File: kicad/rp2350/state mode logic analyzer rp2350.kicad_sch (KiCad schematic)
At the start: 152 parts, among them J1 USB0, J2 5V USB0, J3 Probe_Hi, J4 Probe Power, J5 Probe_Lo, J6 Probe Power, J7 SWD0, SW1 Reset 0, SW2 Boot 0, U1 NCP1117-ADJ_SOT223, U12 SN74LVC8T245, U13 SN74LVC2T45DCUR, U2 RP2350_80QFN, U3 AD5241BRZ1M, U4 SN74LVC8T245, U5 SN74LVC8T245, U6 SN74LVC8T245, U7 IS25LP128F-JBLE, U9 MCP1826S, Y1 ECS-120-18-33-JEM-TR

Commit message: replaced discrete rp2350 with stampxl (schematic only)
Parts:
- removed C1, C2: 27p, Capacitor_SMD:C_0603_1608Metric, symbol Device:C
- removed C13, C15, C16, C17, C18, C25, C26, C27, C28, C29, C30: 100n, Capacitor_SMD:C_0402_1005Metric, symbol Device:C
- removed C14, C34: 4.7u, Capacitor_SMD:C_0402_1005Metric, symbol Device:C
- removed C31: 1u, Capacitor_SMD:C_0603_1608Metric_Pad1.08x0.95mm_HandSolder, symbol Device:C_Small
- removed C32, C33: 4.7u, RP2350_80QFN_minimal:C_0402_1005Metric_small_pads, symbol Device:C
- removed C5: 10u, Capacitor_SMD:C_0805_2012Metric, symbol My Library:C_0805
- removed C6: 1u, Capacitor_SMD:C_0805_2012Metric, symbol My Library:C_0805
- removed D3: 1v1, LED_SMD:LED_1206_3216Metric_Pad1.42x1.75mm_HandSolder, symbol Device:LED_Small_Filled
- removed D7: BZA856AVL, Package_TO_SOT_SMD:SOT-353_SC-70-5, symbol Power_Protection:SP0504BAJT
- removed J1: USB0, Connector_USB:USB_C_Receptacle_GCT_USB4105-xx-A_16P_TopMnt_Horizontal, symbol Connector:USB_C_Receptacle_USB2.0_16P
- removed L1: 3.3u, RP2350_80QFN_minimal:L_pol_2016, symbol Device:L
- removed R10: 1k, Resistor_SMD:R_0603_1608Metric_Pad0.98x0.95mm_HandSolder, symbol Device:R_Small
- removed R12: 0, Resistor_SMD:R_0603_1608Metric_Pad0.98x0.95mm_HandSolder, symbol Device:R
- removed R16, R17: 27, Resistor_SMD:R_0603_1608Metric_Pad0.98x0.95mm_HandSolder, symbol Device:R_Small
- removed R23, R24: 5k1, Resistor_SMD:R_0603_1608Metric_Pad0.98x0.95mm_HandSolder, symbol Device:R_Small
- removed R44: 33, Resistor_SMD:R_0402_1005Metric, symbol Device:R
- removed TP15: TestPoint_Harwin, My Libraries:Harwin-S1751-46-Test-Point, symbol My Library:TestPoint_Harwin
- removed U2: RP2350_80QFN, RP2350_80QFN_minimal:RP2350-QFN-80-1EP_10x10_P0.4mm_EP3.4x3.4mm_ThermalVias, symbol MCU_RaspberryPi_RP2350:RP2350_80QFN
- removed U7: IS25LP128F-JBLE, Package_SO:SOIC-8_5.23x5.23mm_P1.27mm, symbol Memory_Flash:W25Q128JVS
- removed U9: MCP1826S, Package_TO_SOT_SMD:SOT-223, symbol Regulator_Linear:MCP1826S
- removed Y1: ECS-120-18-33-JEM-TR, Crystal:Crystal_SMD_3225-4Pin_3.2x2.5mm, symbol Device:Crystal_GND24
- added D6: BZA856AVL, Package_TO_SOT_SMD:SOT-353_SC-70-5, symbol Power_Protection:SP0504BAJT
- added J1: USB0, Connector_USB:USB_C_Receptacle_GCT_USB4105-xx-A_16P_TopMnt_Horizontal, symbol Connector:USB_C_Receptacle_USB2.0
- added J8: FTDI Header, Connector_PinSocket_2.54mm:PinSocket_1x06_P2.54mm_Vertical, symbol Connector_Generic:Conn_01x06
- added R3, R4: 5k1, Resistor_SMD:R_0603_1608Metric_Pad0.98x0.95mm_HandSolder, symbol Device:R_Small
- added R9: 27, Resistor_SMD:R_0603_1608Metric_Pad0.98x0.95mm_HandSolder, symbol Device:R_Small
- added U2: RP2350_Stamp_XL, RP2xxx_Stamp:RP2xxx_Stamp_XL_THT, symbol RP2xxx_Stamp:RP2350_Stamp_XL
- J7: STANDARD Manufacturer Recommendation -> 01R3466
- R7: value 4k7 -> 1k
- R8: value 4k7 -> 27
- SW1: value Reset 0 -> Reset
- SW2: value Boot 0 -> Boot
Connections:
- net +3V3: now also U2.34 (3.3V); no longer R8.1
- net +5V: now also J8.3 (Pin_3), U2.33 (5V)
- net DN: now also R8.1, U2.35 (USB_D-)
- net DP: now also R9.1, U2.36 (USB_D+)
- net GND: now also D6.2 (A), J1.A1 (GND), J1.A12 (GND), J1.B1 (GND), J1.B12 (GND), J1.S1 (SHIELD), J8.1 (Pin_1), R3.2, R4.2, U2.31 (GND)
- net SWCLK: now also U2.38 (SWCLK)
- net SWD: now also U2.37 (SWDIO)
- net USB_DN: now also R8.2, D6.5 (K), J1.A7 (D-), J1.B7 (D-)
- net USB_DP: now also D6.4 (K), J1.A6 (D+), J1.B6 (D+), R9.2
- net VBUS: now also D6.3 (K), J1.A4 (VBUS), J1.A9 (VBUS), J1.B4 (VBUS), J1.B9 (VBUS)
- net at SW2.1: now also R7.2
- net +1V1: no longer names the net of R7.1
- net +1V1: now also U2.40 (BOOTSEL)
- net Run renamed Reset
- net Reset: now also U2.39 (~{RESET}); no longer R8.2
- new net: J1.B5 (CC2), R4.1
- new net: J1.A5 (CC1), R3.1
- new net UART_RX: J8.4 (Pin_4), U2.2 (GPIO1)
- new net UART_TX: J8.5 (Pin_5), U2.1 (GPIO0)
- no-connect marks 3 -> 8
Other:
- note removed: "Added hidden Pin 4 to MCP1826S Symbol"
- note removed: "MCU (RP2354b)"
- note removed: "Power"
- note removed: "TODO: Add PSRAM"
- moved on the sheet: D4, D5, D8, R1, R2, R41, R42, R43, TP21, TP22

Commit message: remove complicated Vccb supply circuit
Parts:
- added C1, C2: 10u, symbol Device:C_Small
- added C5: 1u, symbol Device:C_Small
- added C6: 1u, Capacitor_SMD:C_0603_1608Metric_Pad1.08x0.95mm_HandSolder, symbol Device:C_Small
- added J9: Vth_select, symbol Connector_Generic:Conn_01x03
- added R10: 3k3, symbol Device:R_Small
- added R11: 1k, symbol Device:R_Small
- added TP1, TP2, TP3, TP4, TP5, TP6: TestPoint_Harwin, My Libraries:Harwin-S1751-46-Test-Point, symbol My Library:TestPoint_Harwin
- D8: value 2040_L0 -> 2350_LED
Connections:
- net SCL is gone; now on net I2C1_SCL: R42.2, TP22.1
- net SDA is gone; now on net I2C1_SDA: R41.2, TP21.1
- net +3V3: now also U3.4 (VDD), U3.5 (~{SHDN}), C6.1, TP3.1; no longer U12.23 (V_{CCB}), U12.24 (V_{CCB}), U13.8 (VCCB), U4.23 (V_{CCB}), U4.24 (V_{CCB}), U5.23 (V_{CCB}), U5.24 (V_{CCB}), U6.23 (V_{CCB}), U6.24 (V_{CCB})
- net +5V: now also U1.3 (VI), C1.1, J9.3 (Pin_3)
- net BUF00: now also U2.46 (GPIO35)
- net BUF01: now also U2.45 (GPIO34)
- net BUF02: now also U2.44 (GPIO33)
- net BUF03: now also U2.43 (GPIO32)
- net BUF04: now also U2.42 (GPIO31)
- net BUF05: now also U2.41 (GPIO30)
- net BUF06: now also U2.30 (GPIO29)
- net BUF07: now also U2.29 (GPIO28)
- net BUF08: now also U2.28 (GPIO27)
- net BUF09: now also U2.27 (GPIO26)
- net BUF10: now also U2.26 (GPIO25)
- net BUF11: now also U2.25 (GPIO24)
- net BUF12: now also U2.24 (GPIO23)
- net BUF13: now also U2.23 (GPIO22)
- net BUF14: now also U2.22 (GPIO21)
- net BUF15: now also U2.21 (GPIO20)
- net BUF16: now also U2.18 (GPIO17)
- net BUF17: now also U2.17 (GPIO16)
- net BUF18: now also U2.16 (GPIO15)
- net BUF19: now also U2.15 (GPIO14)
- net BUF20: now also U2.14 (GPIO13)
- net BUF21: now also U2.13 (GPIO12)
- net BUF22: now also U2.12 (GPIO11)
- net BUF23: now also U2.11 (GPIO10)
- net BUF24: now also U2.10 (GPIO9)
- net BUF25: now also U2.9 (GPIO8)
- net BUF26: now also U2.8 (GPIO7)
- net BUF27: now also U2.7 (GPIO6)
- net BUF28: now also U2.6 (GPIO5)
- net BUF29: now also U2.5 (GPIO4)
- net BUF30: now also U2.4 (GPIO3)
- net BUF31: now also U2.3 (GPIO2)
- net CLK: now also U2.2 (GPIO1), U2.20 (GPIO19)
- net GND: now also U3.10 (GND), U3.11 (VSS), U3.3 (B), U3.8 (AD0), U3.9 (AD1), C1.2, C2.2, C5.2, C6.2, R11.2
- net QUAL: now also U2.1 (GPIO0), U2.19 (GPIO18)
- net UART_RX: now also U2.56 (GPIO45); no longer U2.2 (GPIO1)
- net UART_TX: now also U2.55 (GPIO44); no longer U2.1 (GPIO0)
- net at U3.1 (A): now also TP5.1
- net at U3.12 (O2): now also TP2.1
- net at U3.14 (O1): now also TP1.1
- net at U3.2 (W): now also U1.1 (ADJ), C5.1, R10.2, TP4.1
- net I2C1_SCL: now reaches U3.6 (SCL)
- net I2C1_SCL: now also U2.58 (GPIO47)
- net I2C1_SDA: now reaches U3.7 (SDA)
- net I2C1_SDA: now also U2.57 (GPIO46)
- net Vvar: now reaches U1.2 (VO)
- net Vvar: now also C2.1, J9.1 (Pin_1), R10.1, R11.1, TP6.1
- net 2350_LED: now reaches R43.1
- net 2350_LED: now also U2.53 (GPIO42)
- net Armed: now reaches U2.51 (GPIO40)
- net Armed: now also R1.1
- net Triggered: now reaches U2.52 (GPIO41)
- net Triggered: now also R2.1
- new net Vccb: J9.2 (Pin_2), U12.23 (V_{CCB}), U12.24 (V_{CCB}), U13.8 (VCCB), U4.23 (V_{CCB}), U4.24 (V_{CCB}), U5.23 (V_{CCB}), U5.24 (V_{CCB}), U6.23 (V_{CCB}), U6.24 (V_{CCB})
- no-connect marks 8 -> 13
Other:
- note added: "ADS1015 (from enbaldur)"
- note removed: "I2C0"
- note removed: "TSx - PIO3"
- note removed: "double check I2C"
- moved on the sheet: C23, C24, C3, C4, C7, C8, C9, D1, D2, D4, D5, D6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

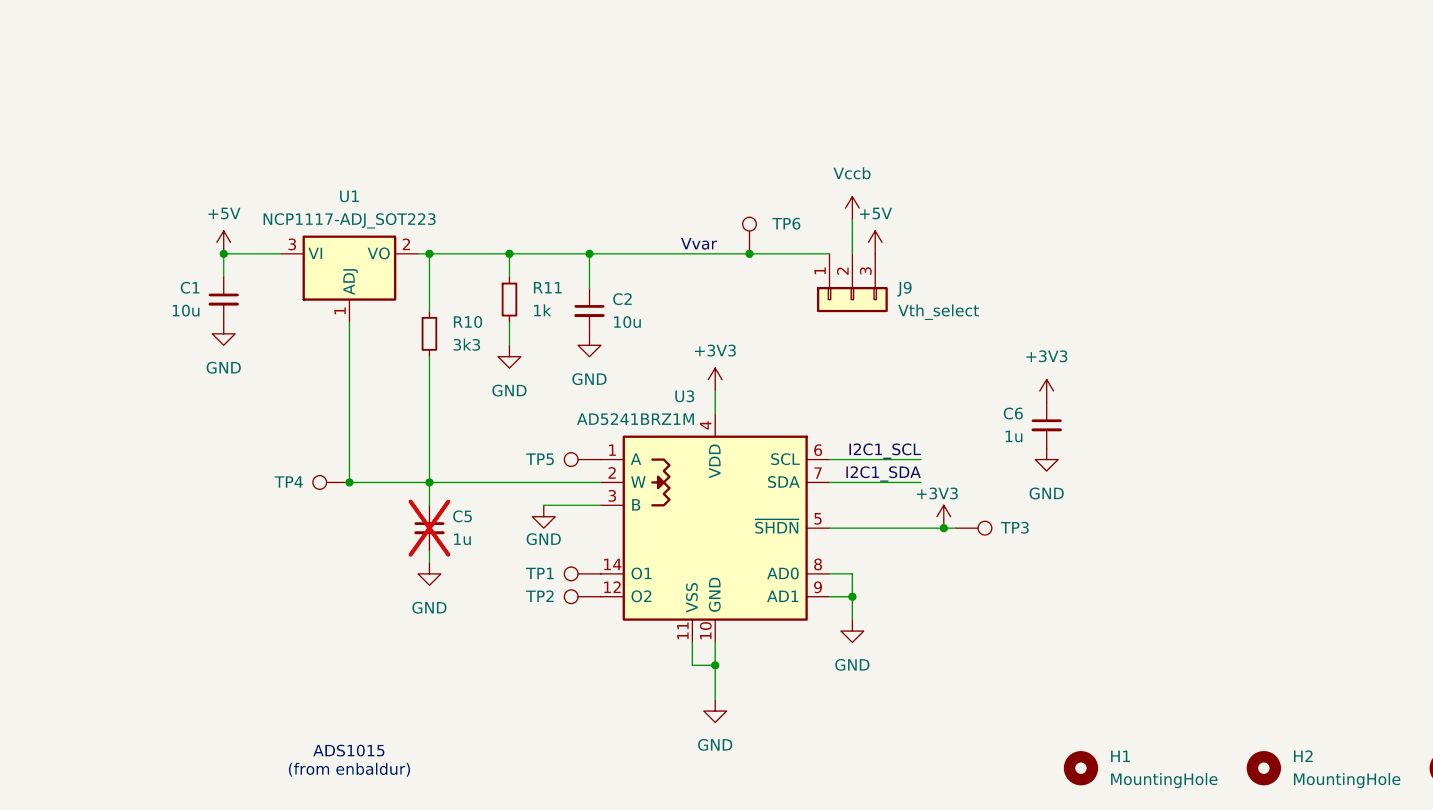
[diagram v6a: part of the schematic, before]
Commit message: drc after adding in Buffered DAC
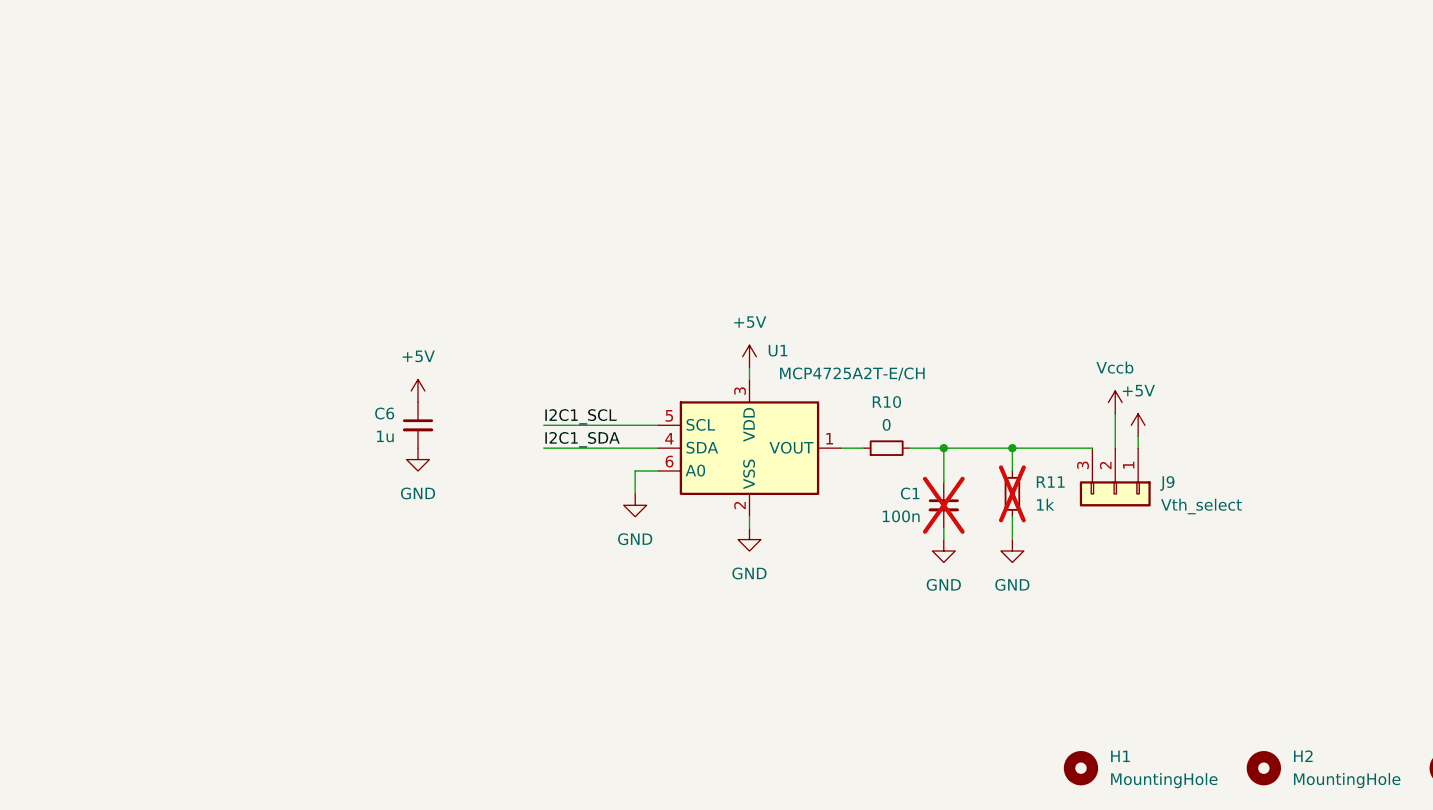
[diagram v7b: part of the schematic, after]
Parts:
- removed C2: 10u, symbol Device:C_Small
- removed C5: 1u, symbol Device:C_Small
- removed TP1, TP2, TP3, TP4, TP5, TP6: TestPoint_Harwin, My Libraries:Harwin-S1751-46-Test-Point, symbol My Library:TestPoint_Harwin
- removed U1: NCP1117-ADJ_SOT223, Package_TO_SOT_SMD:SOT-223-3_TabPin2, symbol Regulator_Linear:NCP1117-ADJ_SOT223
- removed U3: AD5241BRZ1M, Package_SO:SOIC-14_3.9x8.7mm_P1.27mm, symbol My Library:AD5241
- added U1: MCP4725A2T-E/CH, Package_TO_SOT_SMD:SOT-23-6, symbol Analog_DAC:MCP4725xxx-xCH
- C1: value 10u -> 100n; footprint (none) -> Capacitor_SMD:C_0603_1608Metric_Pad1.08x0.95mm_HandSolder; now not fitted
- J9: footprint (none) -> Connector_PinHeader_2.54mm:PinHeader_1x03_P2.54mm_Vertical
- R10: value 3k3 -> 0; footprint (none) -> Resistor_SMD:R_0603_1608Metric
- R11: footprint (none) -> Resistor_SMD:R_0603_1608Metric; now not fitted
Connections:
- net +3V3: no longer C6.1
- net +5V: now also C6.1, J9.1 (Pin_1), U1.3 (VDD); no longer C1.1, J9.3 (Pin_3)
- net GND: now also R11.1, U1.2 (VSS), U1.6 (A0); no longer R11.2
- net I2C1_SCL: now also U1.5 (SCL)
- net I2C1_SDA: now also U1.4 (SDA)
- net at R10.2: now also C1.1, J9.3 (Pin_3), R11.2
- removed net Vvar: J9.1 (Pin_1), R10.1, R11.1
- new net: R10.1, U1.1 (VOUT)
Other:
- note removed: "ADS1015 (from enbaldur)"
- moved on the sheet: C6

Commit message: moving from schematic to pcb
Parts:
- removed R7: 1k, Resistor_SMD:R_0603_1608Metric_Pad0.98x0.95mm_HandSolder, symbol Device:R_Small
- added J10: Vcca_select, symbol Connector_Generic:Conn_01x02
- J9: value Vth_select -> Vccb_select
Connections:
- net +3V3: now also J10.1 (Pin_1); no longer U12.1 (V_{CCA}), U13.1 (VCCA), U4.1 (V_{CCA}), U5.1 (V_{CCA}), U6.1 (V_{CCA})
- net GND: now also U12.2 (DIR), U12.22 (~{OE}), U13.5 (DIR), U4.2 (DIR), U4.22 (~{OE}), U5.2 (DIR), U5.22 (~{OE}), U6.2 (DIR), U6.22 (~{OE})
- net at SW2.1: now also U2.40 (BOOTSEL)
- new net Vcca: J10.2 (Pin_2), U12.1 (V_{CCA}), U13.1 (VCCA), U4.1 (V_{CCA}), U5.1 (V_{CCA}), U6.1 (V_{CCA})
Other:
- moved on the sheet: J2, R8, R9
